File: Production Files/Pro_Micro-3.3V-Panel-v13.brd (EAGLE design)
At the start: 122.9 x 123.7 mm, 579 parts, among them U1 MIC5219, U10 ATMEGA32U4, U11 MIC5219, U12 ATMEGA32U4, U13 MIC5219, U14 ATMEGA32U4, U15 MIC5219, U16 ATMEGA32U4, U17 MIC5219, U18 ATMEGA32U4, U19 MIC5219, U2 MIC5219, U20 ATMEGA32U4, U21 MIC5219, U22 ATMEGA32U4, U23 MIC5219, U24 ATMEGA32U4, U25 MIC5219, U26 ATMEGA32U4, U27 MIC5219, U28 ATMEGA32U4, U29 MIC5219, U3 ATMEGA32U4, U30 ATMEGA32U4, U31 MIC5219, U32 ATMEGA32U4, U33 MIC5219, U34 ATMEGA32U4, U35 MIC5219, U36 ATMEGA32U4, U4 ATMEGA32U4, U5 MIC5219, U6 ATMEGA32U4, U7 MIC5219, U8 ATMEGA32U4, U9 MIC5219, Y1 16MHz, Y10 16MHz, Y11 16MHz, Y12 16MHz, Y13 16MHz, Y14 16MHz, Y15 16MHz, Y16 16MHz, Y17 16MHz, Y18 16MHz, Y2 16MHz, Y3 16MHz, Y4 16MHz, Y5 16MHz, Y6 16MHz, Y7 16MHz, Y8 16MHz, Y9 16MHz

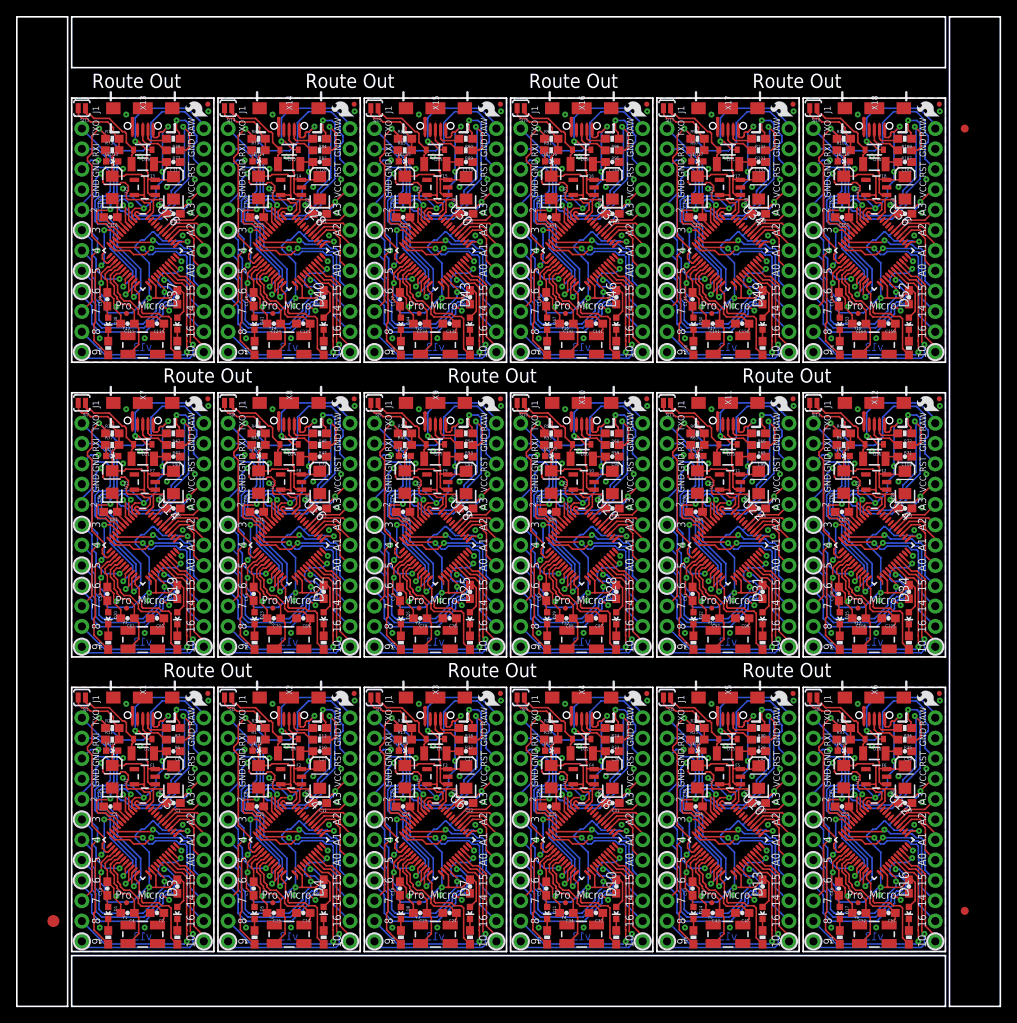
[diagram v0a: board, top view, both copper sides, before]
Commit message: changed tcream on ATmega32U4 to "less paste"
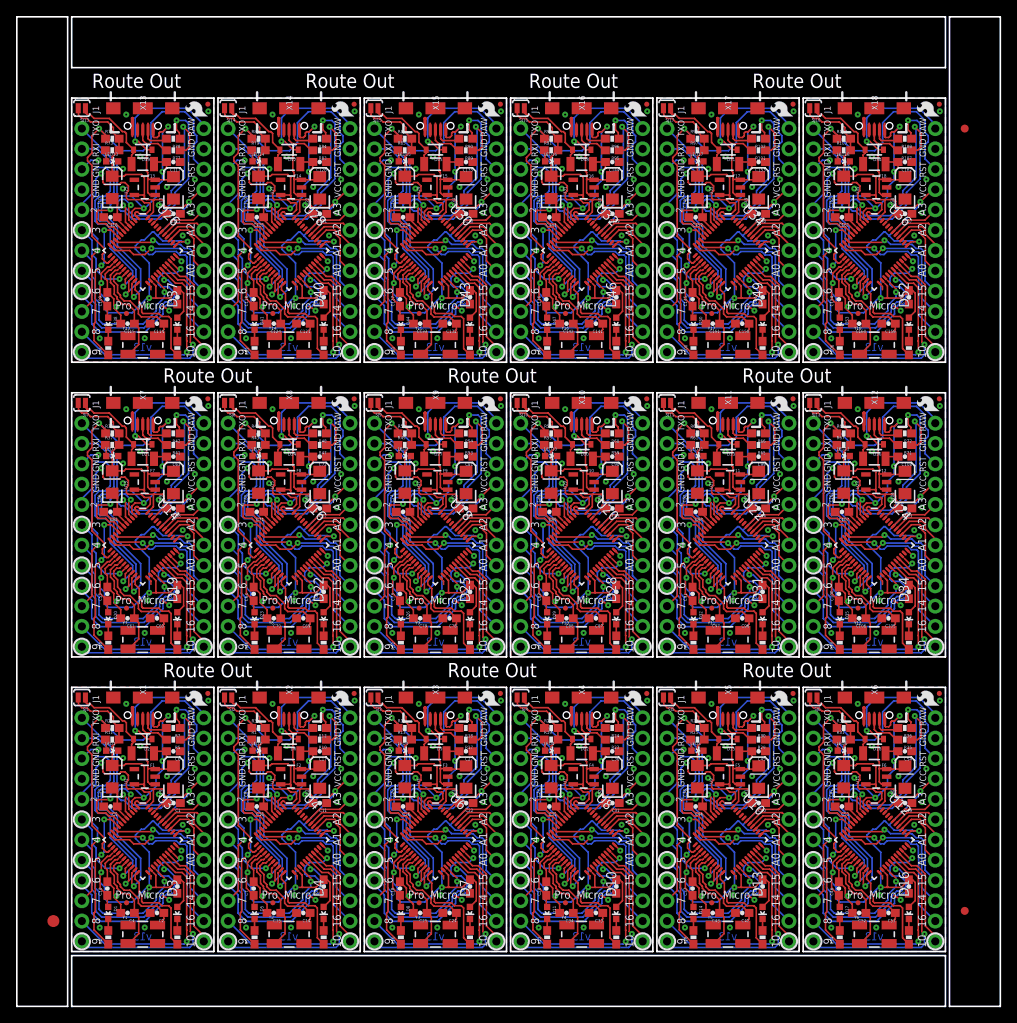
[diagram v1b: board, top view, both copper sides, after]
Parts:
- U10, U12, U14, U16, U18, U20, U22, U24, U26, U28, U3, U30, U32, U34, U36, U4, U6, U8: device Testing:QFN-44-NOPAD_1:1-OUTFAKES -> Testing:QFN-44-NOPAD_1:1-LESS_PASTE
